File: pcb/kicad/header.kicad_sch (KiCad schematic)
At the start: 24 parts, among them J1 Pi 5 GPIO header, J2 Screen PH2.0, J3 Screen 5V/GND pins, J4 To Pi 5 J2 pads, SW1 Power, U5 CAT24C32WI-GT3

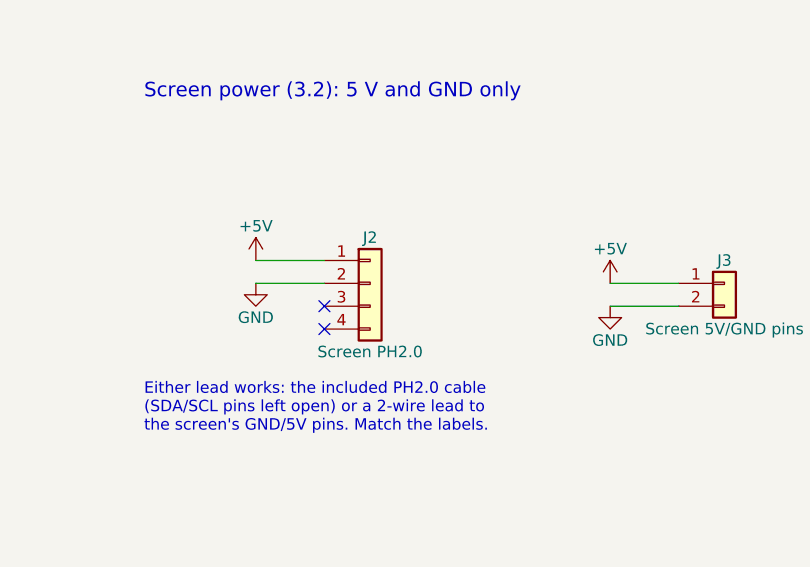
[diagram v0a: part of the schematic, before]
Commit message: Pedalboard PCB: audio converters and clocks sheet
PCM5122 DAC (0x4D, clock master) and PCM1863 ADC (0x4A), wired as the
HiFiBerry DAC+ADC Pro driver expects; Kyocera 22.5792 and 24.576 MHz
oscillators enabled by the DAC's GPIO6/GPIO3 and joined by an OR gate;
DAC output filters and the ADC's input filter from TI's datasheets.

Co-Authored-By: Claude Opus 5.5 <noreply@anthropic.com>
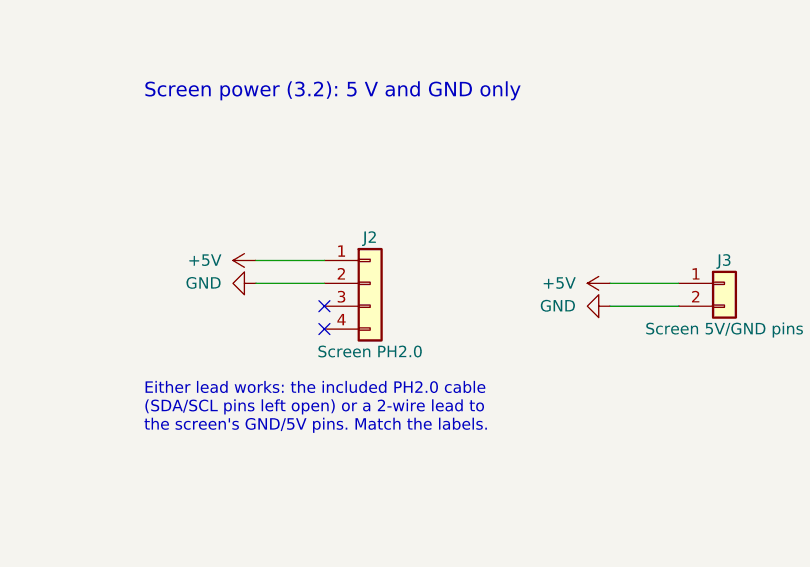
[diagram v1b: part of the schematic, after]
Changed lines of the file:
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@@
 	(symbol
 		(lib_id "power:+5V")
-		(at 312.42 177.8 0)
+		(at 312.42 177.8 90)
 		(unit 1)
 		(exclude_from_sim no)
@@
 		(dnp no)
 		(property "Reference" "#PWR006"
-			(at 312.42 181.61 0)
+			(at 316.23 177.8 90)
 			(effects
 				(font
@@
 		)
 		(property "Value" "+5V"
-			(at 312.42 173.99 0)
-			(effects
-				(font
-					(size 1.27 1.27)
-				)
+			(at 308.61 177.8 90)
+			(effects
+				(font
+					(size 1.27 1.27)
+				)
+				(justify left)
 			)
 		)
 		(property "Footprint" ""
-			(at 312.42 177.8 0)
+			(at 312.42 177.8 90)
 			(effects
 				(font
@@
 		)
 		(property "Datasheet" ""
-			(at 312.42 177.8 0)
+			(at 312.42 177.8 90)
 			(effects
 				(font
@@
 		)
 		(property "Description" "Power symbol creates a global label with name \"+5V\""
-			(at 312.42 177.8 0)
+			(at 312.42 177.8 90)
 			(effects
 				(font
@@
 	(symbol
 		(lib_id "power:GND")
-		(at 312.42 180.34 0)
+		(at 312.42 180.34 270)
 		(unit 1)
 		(exclude_from_sim no)
@@
 		(dnp no)
 		(property "Reference" "#PWR007"
-			(at 312.42 186.69 0)
+			(at 306.07 180.34 90)
 			(effects
 				(font
@@
 		)
 		(property "Value" "GND"
-			(at 312.42 184.15 0)
-			(effects
-				(font
-					(size 1.27 1.27)
-				)
+			(at 308.61 180.34 90)
+			(effects
+				(font
+					(size 1.27 1.27)
+				)
+				(justify right)
 			)
 		)
 		(property "Footprint" ""
-			(at 312.42 180.34 0)
+			(at 312.42 180.34 90)
 			(effects
 				(font
@@
 		)
 		(property "Datasheet" ""
-			(at 312.42 180.34 0)
+			(at 312.42 180.34 90)
 			(effects
 				(font
@@
 		)
 		(property "Description" "Power symbol creates a global label with name \"GND\" , ground"
-			(at 312.42 180.34 0)
+			(at 312.42 180.34 90)
 			(effects
 				(font
@@
 	(symbol
 		(lib_id "power:+5V")
-		(at 351.79 180.34 0)
+		(at 351.79 180.34 90)
 		(unit 1)
 		(exclude_from_sim no)
@@
 		(dnp no)
 		(property "Reference" "#PWR008"
-			(at 351.79 184.15 0)
+			(at 355.6 180.34 90)
 			(effects
 				(font
@@
 		)
 		(property "Value" "+5V"
-			(at 351.79 176.53 0)
-			(effects
-				(font
-					(size 1.27 1.27)
-				)
+			(at 347.98 180.34 90)
+			(effects
+				(font
+					(size 1.27 1.27)
+				)
+				(justify left)
 			)
 		)
 		(property "Footprint" ""
-			(at 351.79 180.34 0)
+			(at 351.79 180.34 90)
 			(effects
 				(font
@@
 		)
 		(property "Datasheet" ""
-			(at 351.79 180.34 0)
+			(at 351.79 180.34 90)
 			(effects
 				(font
@@
 		)
 		(property "Description" "Power symbol creates a global label with name \"+5V\""
-			(at 351.79 180.34 0)
+			(at 351.79 180.34 90)
 			(effects
 				(font
@@
 	(symbol
 		(lib_id "power:GND")
-		(at 351.79 182.88 0)
+		(at 351.79 182.88 270)
 		(unit 1)
 		(exclude_from_sim no)
@@
 		(dnp no)
 		(property "Reference" "#PWR009"
-			(at 351.79 189.23 0)
+			(at 345.44 182.88 90)
 			(effects
 				(font
@@
 		)
 		(property "Value" "GND"
-			(at 351.79 186.69 0)
-			(effects
-				(font
-					(size 1.27 1.27)
-				)
+			(at 347.98 182.88 90)
+			(effects
+				(font
+					(size 1.27 1.27)
+				)
+				(justify right)
 			)
 		)
 		(property "Footprint" ""
-			(at 351.79 182.88 0)
+			(at 351.79 182.88 90)
 			(effects
 				(font
@@
 		)
 		(property "Datasheet" ""
-			(at 351.79 182.88 0)
+			(at 351.79 182.88 90)
 			(effects
 				(font
@@
 		)
 		(property "Description" "Power symbol creates a global label with name \"GND\" , ground"
-			(at 351.79 182.88 0)
-			(effects
-				(font
+			(at 351.79 182.88 90)
+			(effects
+				(font

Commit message: Pedalboard PCB: first layout, and Alps RK09L pots
A 4-layer, 208 x 90 mm board, placed and routed from the netlist: the
jacks, knobs, button and clip LED meet the rear panel at the board edge
(from the makers' drawings), small parts sit at the pins the schematic
names, ground plane on In1, routed with Freerouting. Not finished:
4 nets left unrouted, silkscreen to tidy, 3D check to do.

All three knobs are now Alps RK09L12B0A4S (dual 10k log, M9 thread):
the RK09K had no threaded bushing and Alps makes no 50k log single-gang
RK09L. The gain stage's resistors are scaled by 1/5 to keep the same
gain (simulations A1-A3, A5, A7 re-run: pass, noise 1.0 dB). Footprints
from the symbol libraries are kept (14 parts had none), and the MIDI
jack has its own footprint (pedalboard.pretty).

Co-Authored-By: Claude Opus 5.5 <noreply@anthropic.com>
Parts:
- H1, H2, H3, H4, H5, H6, TP10, TP11, TP12, TP13, TP14, TP8, TP9: now left out of the parts list
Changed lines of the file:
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@@
 		(unit 1)
 		(exclude_from_sim no)
-		(in_bom yes)
+		(in_bom no)
 		(on_board yes)
 		(dnp no)
@@
 		(unit 1)
 		(exclude_from_sim no)
-		(in_bom yes)
+		(in_bom no)
 		(on_board yes)
 		(dnp no)
@@
 		(unit 1)
 		(exclude_from_sim no)
-		(in_bom yes)
+		(in_bom no)
 		(on_board yes)
 		(dnp no)
@@
 		(unit 1)
 		(exclude_from_sim no)
-		(in_bom yes)
+		(in_bom no)
 		(on_board yes)
 		(dnp no)
@@
 		(unit 1)
 		(exclude_from_sim no)
-		(in_bom yes)
+		(in_bom no)
 		(on_board yes)
 		(dnp no)
@@
 		(unit 1)
 		(exclude_from_sim no)
-		(in_bom yes)
+		(in_bom no)
 		(on_board yes)
 		(dnp no)
@@
 		(unit 1)
 		(exclude_from_sim no)
-		(in_bom yes)
+		(in_bom no)
 		(on_board yes)
 		(dnp no)
@@
 		(unit 1)
 		(exclude_from_sim no)
-		(in_bom yes)
+		(in_bom no)
 		(on_board yes)
 		(dnp no)
@@
 		(unit 1)
 		(exclude_from_sim no)
-		(in_bom yes)
+		(in_bom no)
 		(on_board yes)
 		(dnp no)
@@
 		(unit 1)
 		(exclude_from_sim no)
-		(in_bom yes)
+		(in_bom no)
 		(on_board yes)
 		(dnp no)
@@
 		(unit 1)
 		(exclude_from_sim no)
-		(in_bom yes)
+		(in_bom no)
 		(on_board yes)
 		(dnp no)
@@
 		(unit 1)
 		(exclude_from_sim no)
-		(in_bom yes)
+		(in_bom no)
 		(on_board yes)
 		(dnp no)
@@
 		(unit 1)
 		(exclude_from_sim no)
-		(in_bom yes)
-		(on_board yes)
-		(dnp no)
+		(in_bom no)
+		(on_board yes)
+		(dnp no)

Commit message: Pedalboard PCB: maker part numbers and LCSC numbers on every part
Each part on the schematic and the board now carries Manufacturer, MPN
and LCSC fields, for the PCBWay and JLCPCB assembly BOMs. FB1 is the
2 A bead (no 0805 bead is rated 3 A), F1 the MF-MSMF150-2 fuse. The
drill/place origin is the board's bottom-left corner, so the Gerbers,
drill and placement files measure from the board.

Co-Authored-By: Claude Opus 5.5 <noreply@anthropic.com>
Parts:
- C15: LCSC (none) -> C14663; MPN (none) -> CC0603KRX7R9BB104; Manufacturer (none) -> YAGEO
- C16: LCSC (none) -> C12891; MPN (none) -> CL31A226KAHNNNE; Manufacturer (none) -> Samsung
- J1: LCSC (none) -> C132132; MPN (none) -> DS1023-2*20SF11; Manufacturer (none) -> CONNFLY; Note 2x20 female socket, about 8.5 mm tall, on the board's under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 -> 2x20 female socket, 8.5 mm tall, on the board's underside (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
- J2: LCSC (none) -> C131334; MPN (none) -> B4B-PH-K-S(LF)(SN); Manufacturer (none) -> JST
- J3: LCSC (none) -> C492401; MPN (none) -> PZ254V-11-02P; Manufacturer (none) -> XFCN
- J4: LCSC (none) -> C158012; MPN (none) -> B2B-XH-A(LF)(SN); Manufacturer (none) -> JST
- R11, R12: LCSC (none) -> C23018; MPN (none) -> 0603WAF3901T5E; Manufacturer (none) -> UNI-ROYAL
- R13: LCSC (none) -> C21190; MPN (none) -> 0603WAF1001T5E; Manufacturer (none) -> UNI-ROYAL
- SW1: MPN (none) -> PTS645VL83-2 LFS; Manufacturer (none) -> C&K
- U5: LCSC (none) -> C81193; MPN (none) -> CAT24C32WI-GT3; Manufacturer (none) -> onsemi
